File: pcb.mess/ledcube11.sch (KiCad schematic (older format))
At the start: 74 parts, among them P1 LEDCUBE_ROW11, P10 LEDCUBE_ROW11, P11 LEDCUBE_ROW11, P12 LEDCUBE_ROW11, P13 LECUBE_CON1, P14 LEDCUBE_CON2, P15 LEDCUBE_CON3, P2 LEDCUBE_ROW11, P3 LEDCUBE_ROW11, P4 LEDCUBE_ROW11, P5 LEDCUBE_ROW11, P6 LEDCUBE_ROW11, P7 LEDCUBE_ROW11, P8 LEDCUBE_ROW11, P9 LEDCUBE_ROW11, T1 ZXMP4A16, T10 ZXMP4A16, T11 ZXMP4A16, T2 ZXMP4A16, T3 ZXMP4A16, T4 ZXMP4A16, T5 ZXMP4A16, T6 ZXMP4A16, T7 ZXMP4A16, T8 ZXMP4A16, T9 ZXMP4A16, U1 TLC5941, U2 TLC5941, U3 TLC5941, U4 TLC5941, U5 TLC5941, U6 TLC5941, U7 TLC5941, U8 TLC5941

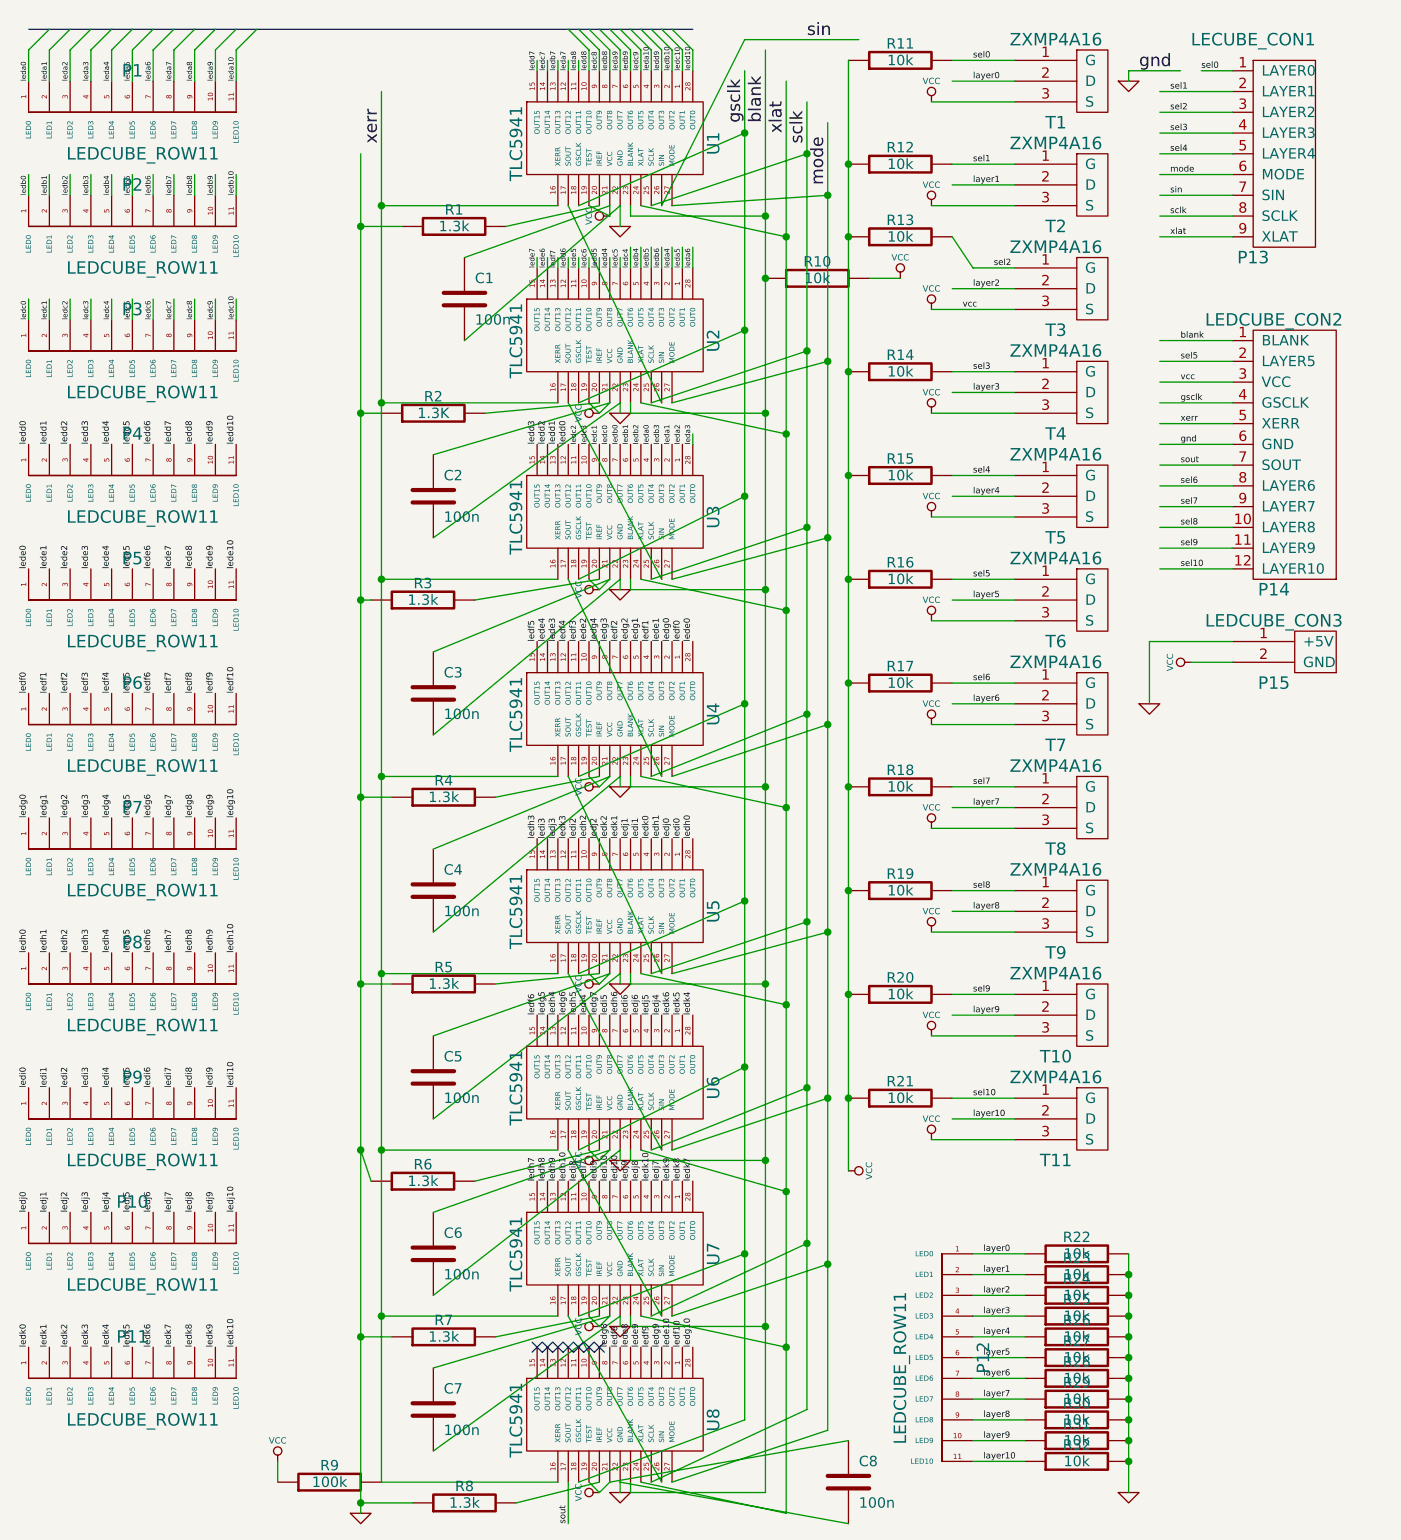
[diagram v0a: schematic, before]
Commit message: Updated print: misc. tweaks; separate LED and TLC5940 power supply; squeeze width to (hopefully) fit PCB cutter.
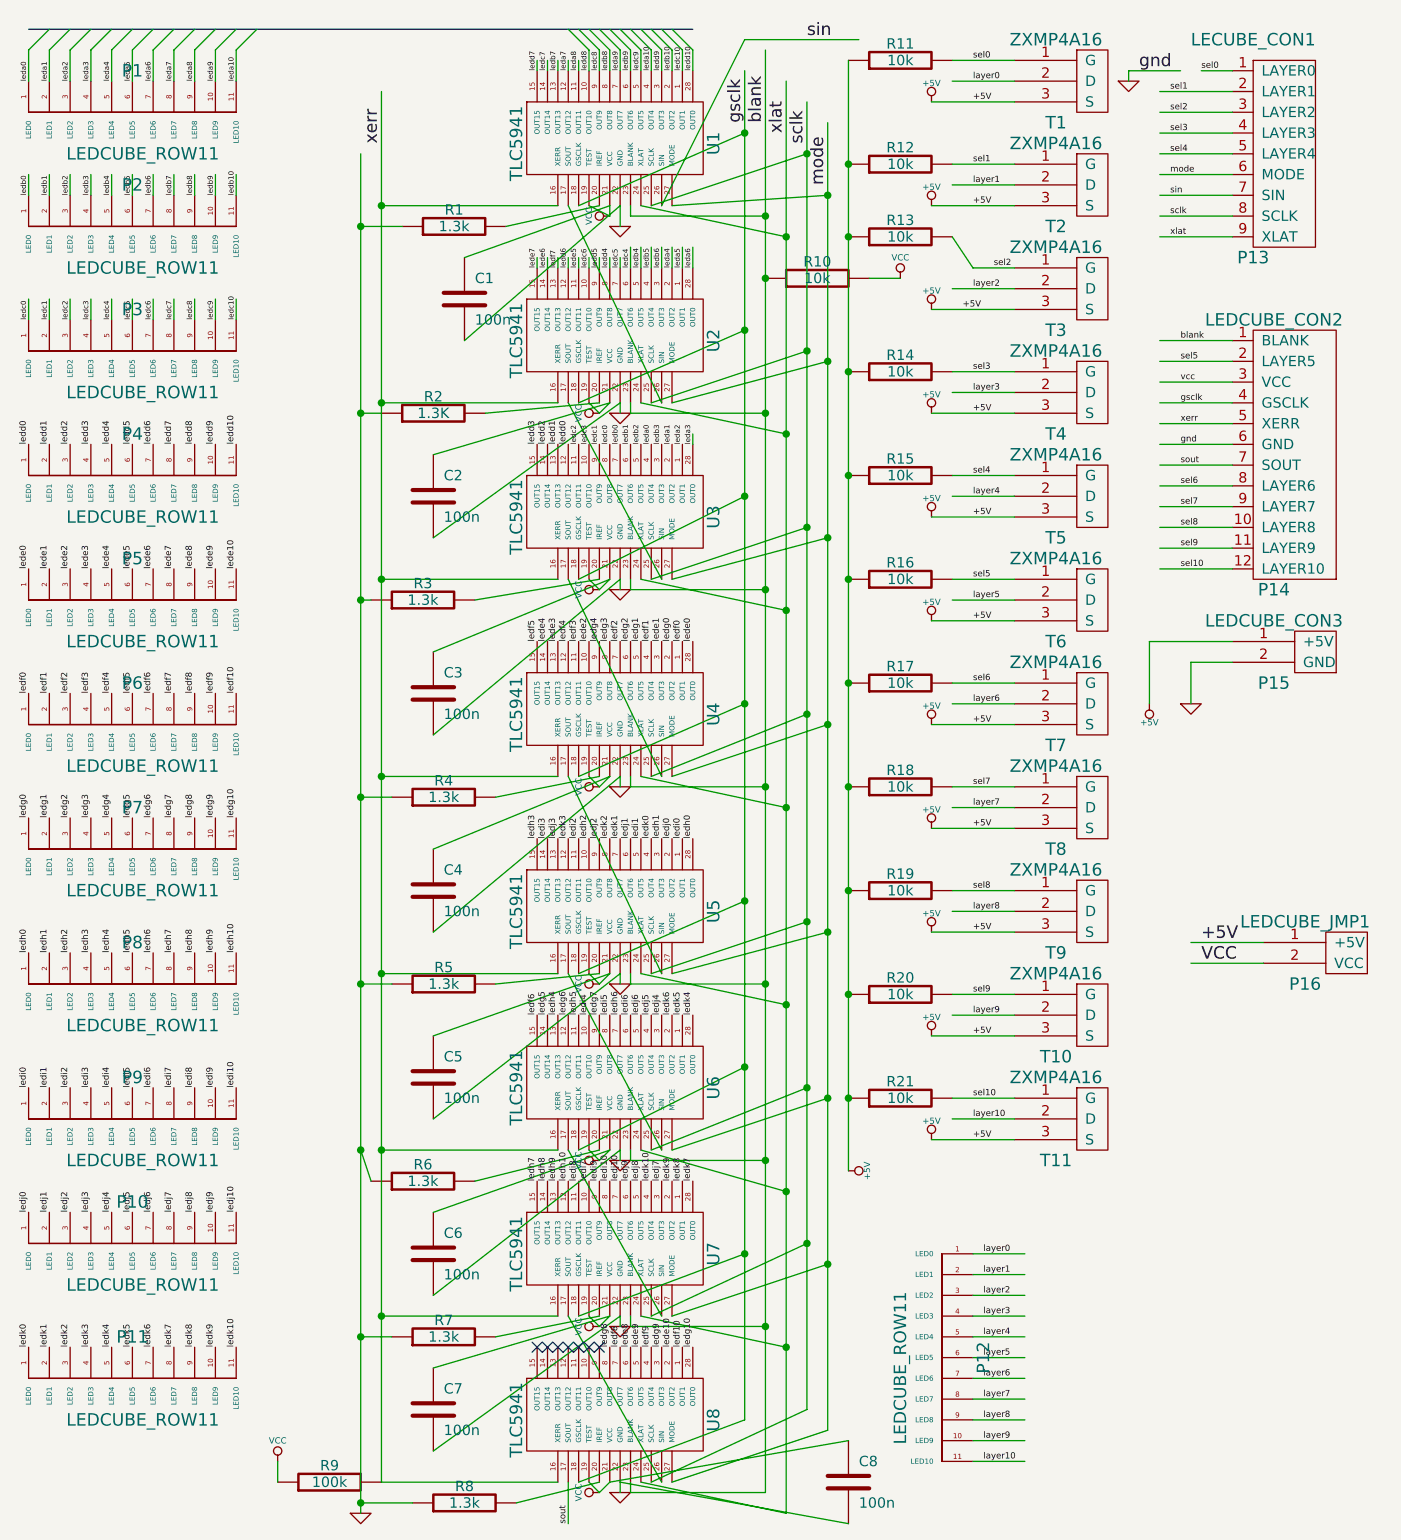
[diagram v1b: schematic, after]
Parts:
- removed R22, R23, R24, R25, R26, R27, R28, R29, R30, R31, R32: 10k, symbol R
- added P16: LEDCUBE_JMP1, symbol LEDCUBE_JMP1
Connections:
- net labels added: +5V
- wire segments 270 -> 272
